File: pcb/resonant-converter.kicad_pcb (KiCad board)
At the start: 4 copper layers, 100 x 100 mm, 112 parts, among them J1 Banana_Jack_Keystone_575-8, J2 Banana_Jack_Keystone_575-8, J3 Banana_Jack_Keystone_575-8, J4 Banana_Jack_Keystone_575-8, J5 JST_SH_1x4_BM04B-SRSS-TB-LF-SN, J6 Molex_KK_1x4_0470531000, Q1 MDU04N010VRH, Q2 MDU04N010VRH, Q3 HSU30N20, Q4 HSU30N20, T1 B66206W1110T001, U1 UCC256610DDBR, U2 TEA2096T/1J, U3 INA219BIDCNR, U4 PC817X2CSP9F, U5 TL431AIDBVR, U6 78L15MG

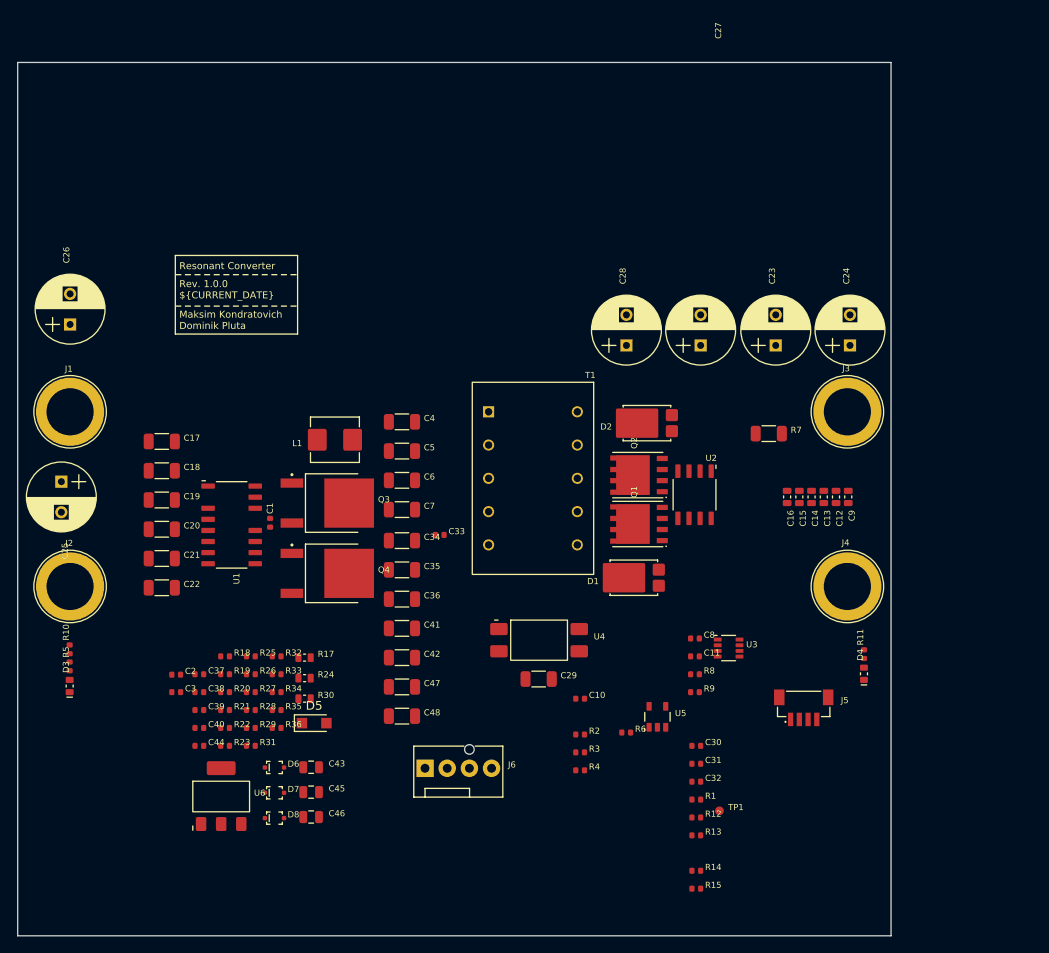
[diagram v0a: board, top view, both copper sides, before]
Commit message: Re-annotate schematic, update PCB from schematic
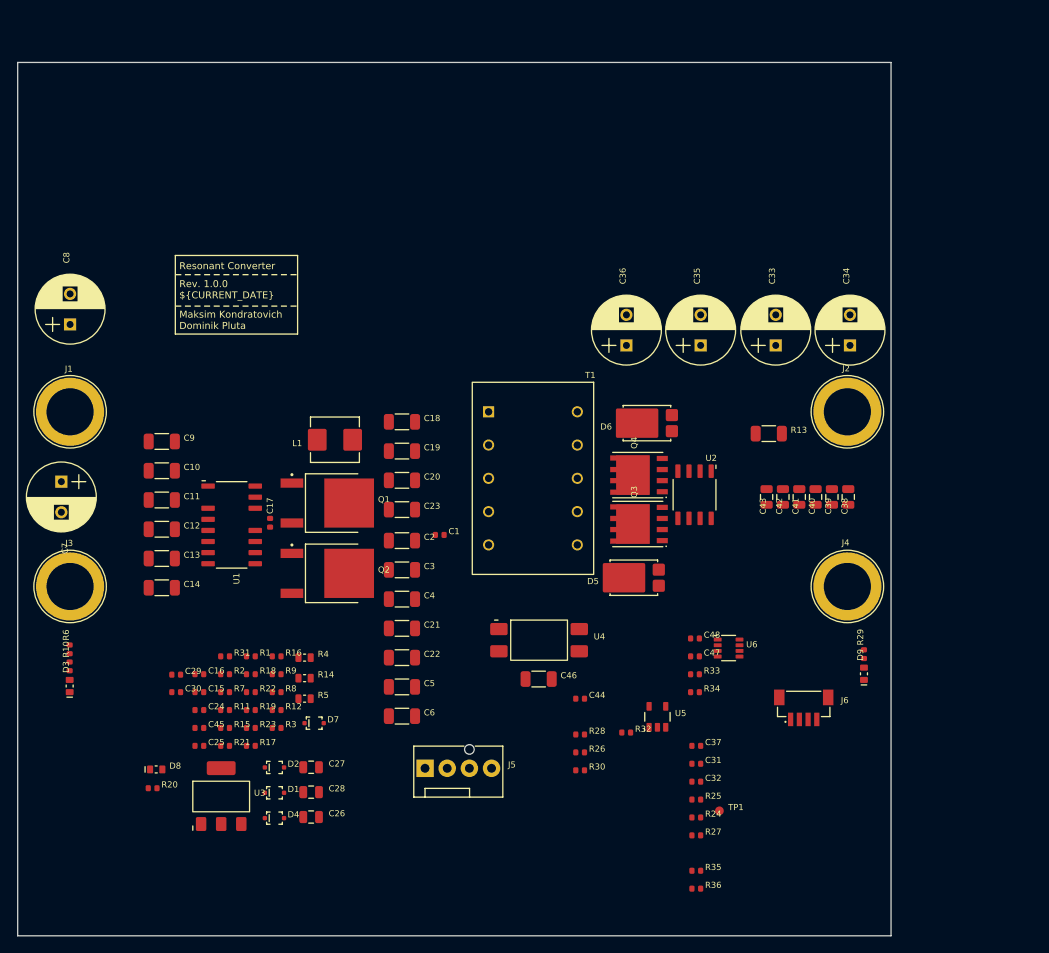
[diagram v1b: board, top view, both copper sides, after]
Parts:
- added D8: LED-R-0603_KT-0603R, DW-footprints:LED_0603_1608Metric_R, F.Cu at (115.9, 130.9)
- added R20: R-10k-0402, DW-footprints:R_0402_1005Metric, F.Cu at (115.5, 133.1)
- C38: renamed from C9; value C-10u-0603 -> C-10u-0805; footprint DW-footprints:C_0603_1608Metric -> DW-footprints:C_0805_2012Metric
- C39: renamed from C12; value C-10u-0603 -> C-10u-0805; footprint DW-footprints:C_0603_1608Metric -> DW-footprints:C_0805_2012Metric
- C40: renamed from C13; value C-10u-0603 -> C-10u-0805; footprint DW-footprints:C_0603_1608Metric -> DW-footprints:C_0805_2012Metric
- C41: renamed from C14; value C-10u-0603 -> C-10u-0805; footprint DW-footprints:C_0603_1608Metric -> DW-footprints:C_0805_2012Metric
- C42: renamed from C15; value C-10u-0603 -> C-10u-0805; footprint DW-footprints:C_0603_1608Metric -> DW-footprints:C_0805_2012Metric
- C43: renamed from C16; value C-10u-0603 -> C-10u-0805; footprint DW-footprints:C_0603_1608Metric -> DW-footprints:C_0805_2012Metric
- D7: renamed from D5; value PMEG10020AELR -> 1N4148WS-AU; footprint Diode_SMD:Nexperia_CFP3_SOD-123W -> DW-footprints:D_SOD-323F
- moved C43 2.35 mm to (185.8, 99.8)
- moved C42 1.88 mm to (187.6, 99.8)
- moved C41 1.41 mm to (189.5, 99.8)
- moved C40 0.94 mm to (191.4, 99.8)
- moved C39 0.47 mm to (193.2, 99.8)
- renumbered C33 to C1, C18 to C10, C19 to C11, C20 to C12, C21 to C13, C22 to C14, C38 to C15, C37 to C16, C1 to C17, C4 to C18, C5 to C19, C34 to C2, C6 to C20, C41 to C21, C42 to C22, C7 to C23, C39 to C24, C44 to C25, C46 to C26, C43 to C27, C45 to C28, C2 to C29, C35 to C3, C3 to C30, C23 to C33, C24 to C34, C27 to C35, C28 to C36, C30 to C37, C36 to C4, C10 to C44, C40 to C45, C29 to C46, C11 to C47, C8 to C48, C47 to C5, C48 to C6, C25 to C7, C26 to C8, C17 to C9, D7 to D1, D6 to D2, D8 to D4, D1 to D5, D2 to D6, D4 to D9, J3 to J2, J2 to J3, J6 to J5, J5 to J6, Q3 to Q1, Q4 to Q2, Q1 to Q3, Q2 to Q4, R25 to R1, R5 to R10, R21 to R11, R35 to R12, R7 to R13, R24 to R14, R22 to R15, R32 to R16, R31 to R17, R26 to R18, R28 to R19, R19 to R2, R23 to R21, R27 to R22, R29 to R23, R12 to R24, R1 to R25, R3 to R26, R13 to R27, R2 to R28, R11 to R29, R36 to R3, R4 to R30, R18 to R31, R6 to R32, R8 to R33, R9 to R34, R14 to R35, R15 to R36, R17 to R4, R30 to R5, R10 to R6, R20 to R7, R34 to R8, R33 to R9, U6 to U3, U3 to U6
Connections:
- net Net-(D8-C) renamed /LO
- net Net-(Q3-S) renamed /HS
- net Net-(U1-HB) renamed /HB
- D2 pad 1: Net-(D6-C) (its old number) -> /HO
- R8 pad 1: Net-(D6-C) (its old number) -> /HO
- U1 pad 15: Net-(D6-C) (its old number) -> /HO

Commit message: PCB: Update PCB from schematic, layout power monitor section
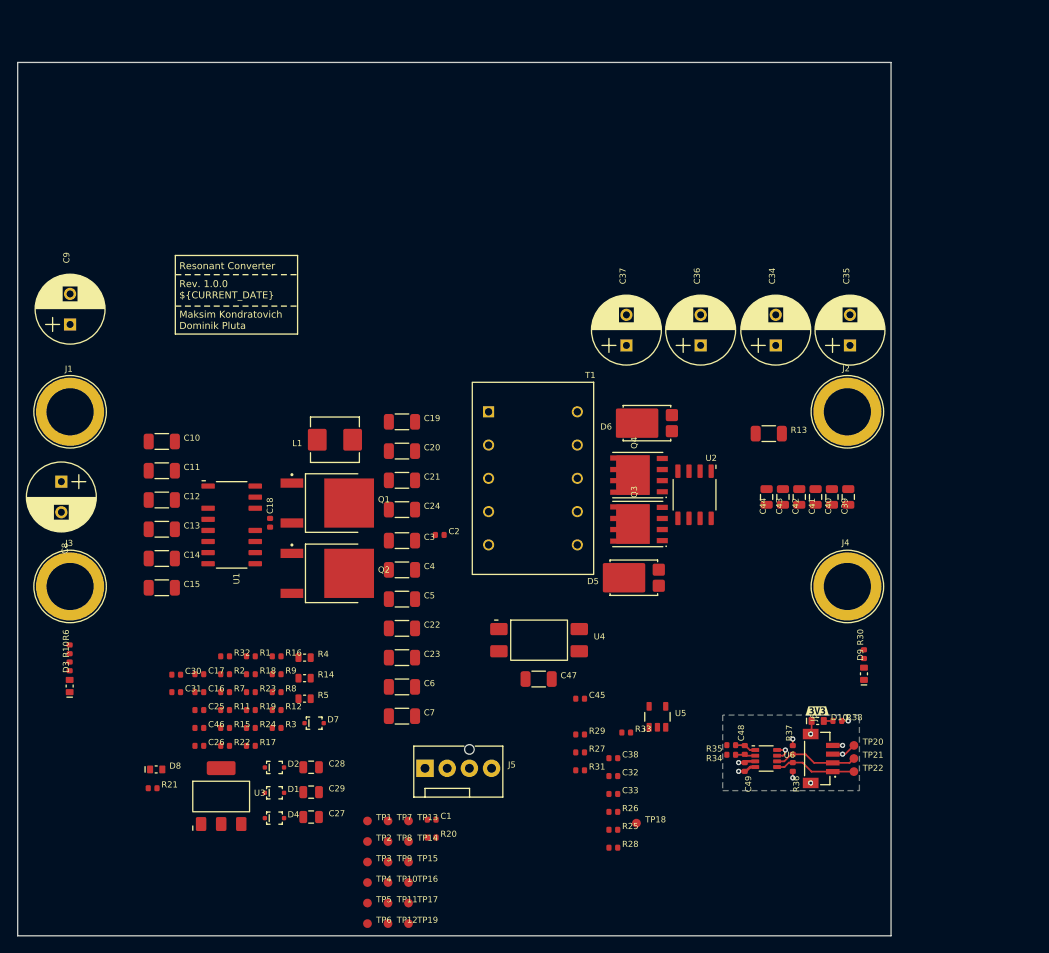
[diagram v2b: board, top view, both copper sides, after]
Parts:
- added C1: C-1u-0402, DW-footprints:C_0402_1005Metric, F.Cu at (147.4, 136.7)
- added D10: LED-R-0603_KT-0603R, DW-footprints:LED_0603_1608Metric_R, F.Cu at (191.6, 125.4)
- added R20: R-0R-0402, DW-footprints:R_0402_1005Metric, F.Cu at (147.4, 138.8)
- added R38: R-470R-0402, DW-footprints:R_0402_1005Metric, F.Cu at (193.8, 125.4)
- added TP1: TP_SMD_1mm, DW-footprints:TP_SMD_1mm, F.Cu at (140.1, 136.8)
- added TP10: TP_SMD_1mm, DW-footprints:TP_SMD_1mm, F.Cu at (142.4, 143.9)
- added TP11: TP_SMD_1mm, DW-footprints:TP_SMD_1mm, F.Cu at (142.4, 146.2)
- added TP12: TP_SMD_1mm, DW-footprints:TP_SMD_1mm, F.Cu at (142.4, 148.6)
- added TP13: TP_SMD_1mm, DW-footprints:TP_SMD_1mm, F.Cu at (144.8, 136.8)
- added TP14: TP_SMD_1mm, DW-footprints:TP_SMD_1mm, F.Cu at (144.8, 139.2)
- added TP15: TP_SMD_1mm, DW-footprints:TP_SMD_1mm, F.Cu at (144.8, 141.6)
- added TP16: TP_SMD_1mm, DW-footprints:TP_SMD_1mm, F.Cu at (144.8, 143.9)
- added TP17: TP_SMD_1mm, DW-footprints:TP_SMD_1mm, F.Cu at (144.8, 146.2)
- added TP19: TP_SMD_1mm, DW-footprints:TP_SMD_1mm, F.Cu at (144.8, 148.6)
- added TP2: TP_SMD_1mm, DW-footprints:TP_SMD_1mm, F.Cu at (140.1, 139.2)
- added TP20: TP_SMD_1mm, DW-footprints:TP_SMD_1mm, F.Cu at (195.8, 128.2)
- added TP21: TP_SMD_1mm, DW-footprints:TP_SMD_1mm, F.Cu at (195.8, 129.7)
- added TP22: TP_SMD_1mm, DW-footprints:TP_SMD_1mm, F.Cu at (195.8, 131.2)
- added TP3: TP_SMD_1mm, DW-footprints:TP_SMD_1mm, F.Cu at (140.1, 141.6)
- added TP4: TP_SMD_1mm, DW-footprints:TP_SMD_1mm, F.Cu at (140.1, 143.9)
- added TP5: TP_SMD_1mm, DW-footprints:TP_SMD_1mm, F.Cu at (140.1, 146.2)
- added TP6: TP_SMD_1mm, DW-footprints:TP_SMD_1mm, F.Cu at (140.1, 148.6)
- added TP7: TP_SMD_1mm, DW-footprints:TP_SMD_1mm, F.Cu at (142.4, 136.8)
- added TP8: TP_SMD_1mm, DW-footprints:TP_SMD_1mm, F.Cu at (142.4, 139.2)
- added TP9: TP_SMD_1mm, DW-footprints:TP_SMD_1mm, F.Cu at (142.4, 141.6)
- added kibuzzard-69E92ECD: G***, kibuzzard-69E92ECD, F.Cu at (191.6, 124.2)
- C2: renamed from C1; value 4.7n -> 4n7
- moved R37 19.3 mm to (188.8, 128.7), turned to 90 degrees
- moved R36 16.2 mm to (188.8, 130.7), turned to -90 degrees
- moved C49 15.8 mm to (183.2, 130.7), turned to -90 degrees
- moved U6 13.4 mm to (185.7, 129.7)
- moved C48 12.1 mm to (183.2, 128.7), turned to 90 degrees
- moved R34 10.1 mm to (181.7, 129.3), turned to 180 degrees
- moved R25 9.60 mm to (168.2, 137.9)
- moved C32 9.60 mm to (168.2, 131.7)
- moved C33 9.60 mm to (168.2, 133.8)
- moved C38 9.60 mm to (168.2, 129.7)
- moved R26 9.60 mm to (168.2, 135.8)
- moved R28 9.60 mm to (168.2, 139.9)
- moved TP18 9.60 mm to (170.8, 137.1)
- moved R35 7.35 mm to (181.7, 128.2), turned to 180 degrees
- moved J6 6.44 mm to (191.6, 129.7), turned to 90 degrees
- renumbered C9 to C10, C10 to C11, C11 to C12, C12 to C13, C13 to C14, C14 to C15, C15 to C16, C16 to C17, C17 to C18, C18 to C19, C19 to C20, C20 to C21, C21 to C22, C22 to C23, C23 to C24, C24 to C25, C25 to C26, C26 to C27, C27 to C28, C28 to C29, C2 to C3, C29 to C30, C30 to C31, C31 to C32, C32 to C33, C33 to C34, C34 to C35, C35 to C36, C36 to C37, C37 to C38, C38 to C39, C3 to C4, C39 to C40, C40 to C41, C41 to C42, C42 to C43, C43 to C44, C44 to C45, C45 to C46, C46 to C47, C47 to C48, C48 to C49, C4 to C5, C5 to C6, C6 to C7, C7 to C8, C8 to C9, R20 to R21, R21 to R22, R22 to R23, R23 to R24, R24 to R25, R25 to R26, R26 to R27, R27 to R28, R28 to R29, R29 to R30, R30 to R31, R31 to R32, R32 to R33, R33 to R34, R34 to R35, R35 to R36, R36 to R37, TP1 to TP18
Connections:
- U3 pad 1: VCCP -> Net-(U3-OUT)
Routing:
- net /Power monitor/SDA: track 0.00 -> 9.75 mm
- net /Power monitor/SCL: track 0.00 -> 9.44 mm
- net +3V3: track 0.00 -> 7.19 mm, vias 0 -> 5
- net GND_ISO: track 0.00 -> 7.02 mm, vias 0 -> 5
- net Net-(U6-IN+): track 0.00 -> 2.48 mm
- net Net-(U6-IN-): track 0.00 -> 2.33 mm
- net Net-(D10-A): track 0.00 -> 1.05 mm
- added copper zone on B.Cu, net +3V3
- added copper zone on In1.Cu, net GND_ISO
- added copper zone on In2.Cu, net GND_ISO
- removed copper zone on In1.Cu, net GND
- removed copper zone on In2.Cu, net GND

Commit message: PCB: Perform initial component placement
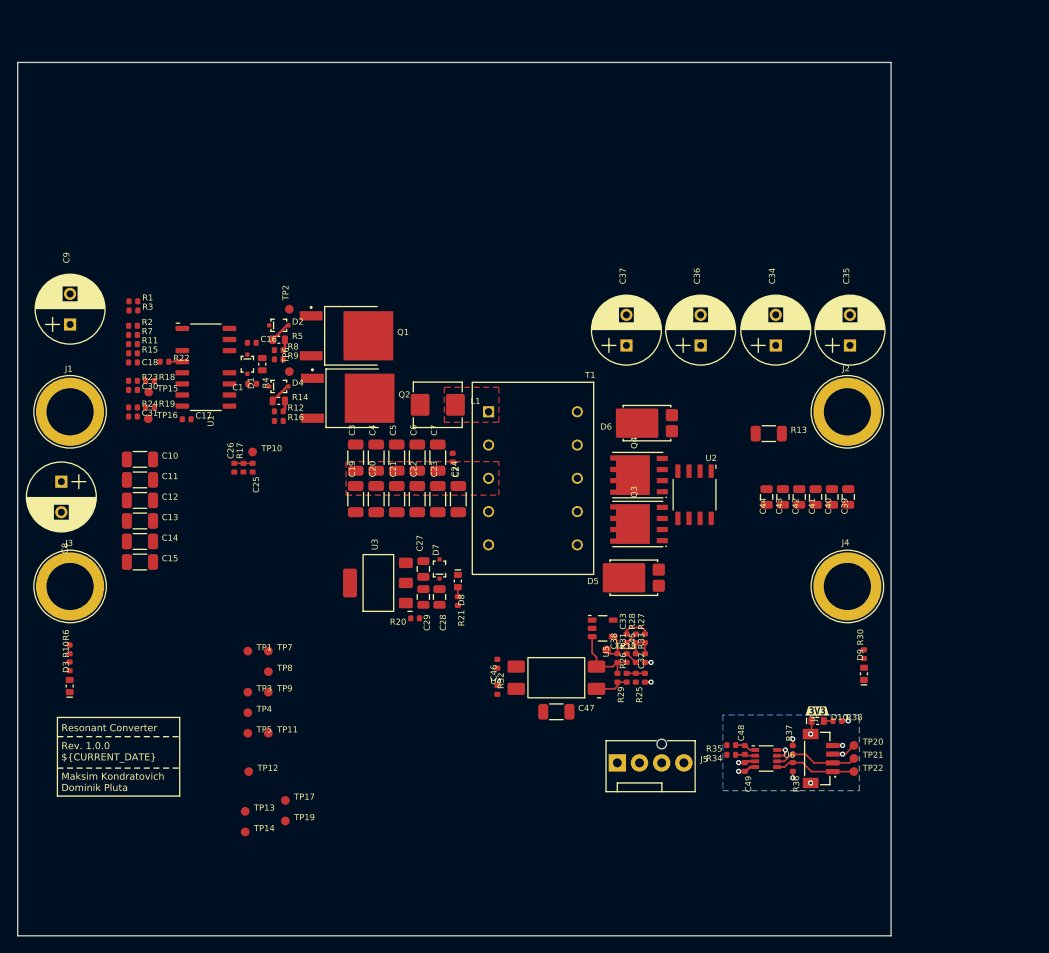
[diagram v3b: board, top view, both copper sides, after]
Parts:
- moved TP6 63.8 mm to (131.1, 85.4), turned to 90 degrees
- moved TP2 61.6 mm to (131.1, 78.2), turned to 90 degrees
- moved TP15 61.5 mm to (115.0, 87.8)
- moved TP16 60.9 mm to (115.0, 90.8)
- moved C1 54.0 mm to (126.8, 86.8), turned to 180 degrees
- moved TP10 51.7 mm to (126.9, 94.6)
- moved D2 50.6 mm to (129.9, 80.1)
- moved R3 50.5 mm to (113.2, 78.4)
- moved D4 49.4 mm to (129.9, 87.1)
- moved D1 49.2 mm to (126.3, 84.6), turned to -90 degrees
- moved R22 44.5 mm to (116.8, 84.3)
- moved R15 44.2 mm to (113.2, 83.3)
- moved R11 43.2 mm to (113.2, 82.2)
- moved R1 42.8 mm to (113.2, 77.3)
- moved R7 42.2 mm to (113.2, 81.2)
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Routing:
- net /V_FB: track 0.00 -> 8.64 mm
- net Net-(U5-K): track 0.00 -> 8.24 mm
- net Net-(R26-Pad1): track 0.00 -> 4.03 mm
- net +12V: track 0.00 -> 3.19 mm
- net Net-(D4-A): track 0.00 -> 2.48 mm
- net Net-(D2-A): track 0.00 -> 2.48 mm
- net /ISNS: track 0.00 -> 2.10 mm
- net Net-(C32-Pad2): track 0.00 -> 2.10 mm
- net /OVP/OTP: track 0.00 -> 1.55 mm
- net Net-(C45-Pad1): track 0.00 -> 1.46 mm
- net Net-(C33-Pad1): track 0.00 -> 1.46 mm
- net GND_ISO: track 7.02 -> 8.42 mm, vias 5 -> 7
- net Net-(Q2-G): track 0.00 -> 1.28 mm
- net Net-(Q1-G): track 0.00 -> 1.28 mm
- net Net-(D8-A): track 0.00 -> 1.09 mm
- added copper zone on F.Cu, net /TRAFO_BOT
- added copper zone on F.Cu, net /TRAFO_TOP

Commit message: Add mounting holes, fix 4n7 capacitor size
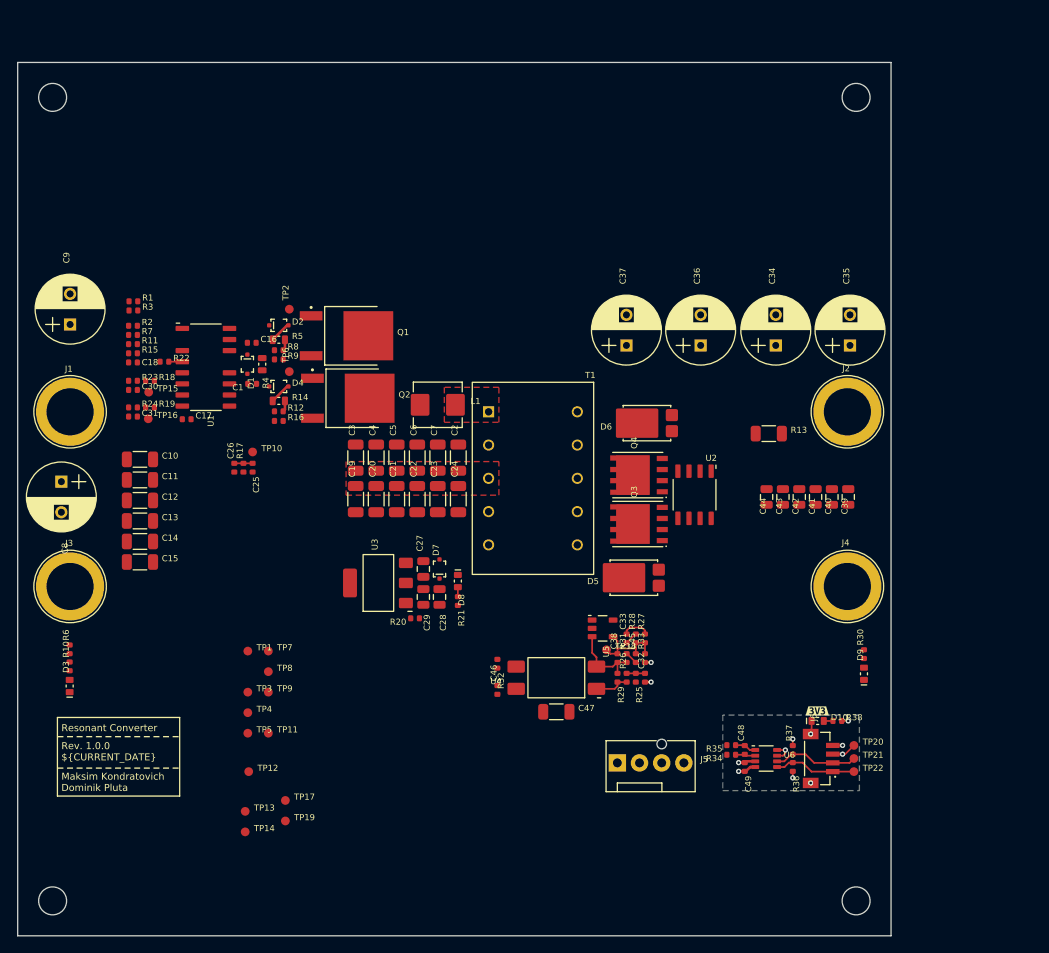
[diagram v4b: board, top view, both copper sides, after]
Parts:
- added REF**: NPTH_3.2mm, DW-footprints:NPTH_3.2mm, F.Cu at (104.0, 146.0)
- added REF**: NPTH_3.2mm, DW-footprints:NPTH_3.2mm, F.Cu at (104.0, 54.0)
- added REF**: NPTH_3.2mm, DW-footprints:NPTH_3.2mm, F.Cu at (196.0, 54.0)
- added REF**: NPTH_3.2mm, DW-footprints:NPTH_3.2mm, F.Cu at (196.0, 146.0)
- C2: value 4n7 -> C-4n7-100V-NP0-1206; footprint DW-footprints:C_0402_1005Metric -> DW-footprints:C_1206_3216Metric
- moved C2 0.65 mm to (150.4, 95.2), turned to 90 degrees
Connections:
- C2 pad 1: +60V -> /TRAFO_BOT
- C2 pad 2: /TRAFO_BOT -> +60V

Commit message: Completed primary side PCB layout
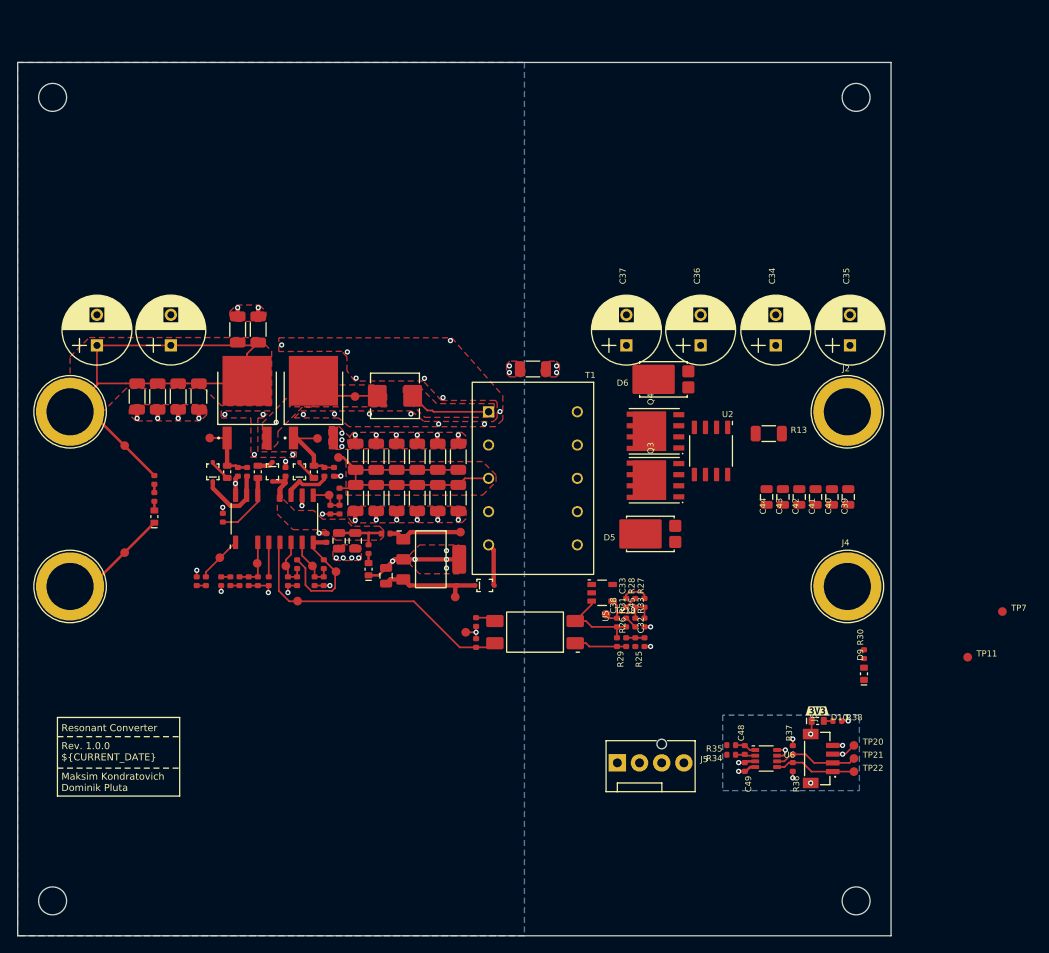
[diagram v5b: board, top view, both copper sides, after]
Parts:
- moved TP7 84.2 mm to (212.8, 112.9)
- moved TP11 80.5 mm to (208.8, 118.1)
- moved TP13 40.4 mm to (150.7, 103.8)
- moved C47 39.3 mm to (159.0, 85.1)
- moved TP14 36.1 mm to (150.1, 111.2)
- moved TP3 36.0 mm to (138.6, 88.2)
- moved R1 32.9 mm to (120.5, 109.4), turned to -90 degrees
- moved R3 32.1 mm to (121.5, 109.4), turned to 90 degrees
- moved R2 30.9 mm to (123.3, 109.4), turned to -90 degrees
- moved R7 30.3 mm to (124.3, 109.4), turned to 90 degrees
- moved TP19 29.9 mm to (151.3, 115.2)
- moved R11 29.8 mm to (125.4, 109.4), turned to -90 degrees
- moved R15 29.3 mm to (126.5, 109.4), turned to 90 degrees
- moved R23 29.0 mm to (130.9, 109.4), turned to 90 degrees
- moved C30 28.9 mm to (132.0, 109.4), turned to 90 degrees
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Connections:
- T1 pad 4: /TRAFO_AUX -> GND
- T1 pad 5: GND -> /TRAFO_AUX
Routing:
- net +60V: track 0.00 -> 74.2 mm, vias 0 -> 8
- net GND: track 0.00 -> 51.8 mm, vias 0 -> 52
- net /TRAFO_BOT: track 0.00 -> 33.5 mm
- net /FB: track 0.00 -> 33.2 mm
- net /HS: track 0.00 -> 23.3 mm, vias 0 -> 3
- net /V5P: track 0.00 -> 14.8 mm
- net Net-(D7-C): track 0.00 -> 12.1 mm
- net VCCP: track 0.00 -> 10.2 mm
- net /TRAFO_TOP: track 0.00 -> 9.45 mm
- net Net-(U3-OUT): track 0.00 -> 8.68 mm
- net /HO: track 0.00 -> 8.42 mm
- net Net-(Q2-G): track 1.28 -> 9.50 mm
- net /HB: track 0.00 -> 7.71 mm
- net /TSET: track 0.00 -> 6.54 mm
- net /LL: track 0.00 -> 6.30 mm
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- added copper zone on F.Cu, net +60V
- added copper zone on In2.Cu, net +60V
- added copper zone on F.Cu, net /HS
- added copper zone on B.Cu, net GND
- added copper zone on F.Cu, net GND
- added copper zone on In1.Cu, net GND
- added copper zone on In2.Cu, net GND
- added copper zone on F.Cu, net GND_ISO
- added copper zone on F.Cu, net VCCP
